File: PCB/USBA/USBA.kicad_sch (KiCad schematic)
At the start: 19 parts, among them J1 USB_A, J2 Shelly, U1 ESP32-PICO-MINI-02, U2 LMR16006+FB, U4 QR

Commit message: New layout for production
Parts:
- removed D1: RGB, RevK:LED-RGB-1.6x1.6, symbol Device:LED_ARGB
- removed U2: LMR16006+FB, RevK:SOT-23-Thin-6-Reg, symbol RevK:LMR16006+FB
- added D1: LED_BARG, RevK:MHS190RGBCT, symbol Device:LED_BARG
- added U2: LMR16006YDDCR, RevK:SOT-23-Thin-6-Reg, symbol RevK:LMR16006XDDCR
- C1: value 0.1uF -> 100nF; LCSC Part # (none) -> C30926; Part No 0603-100nF-50V -> (none)
- C2: LCSC Part # (none) -> C19110; Note 0603 or 0805 -> (none); Part No 0805-2.2uF-25V -> (none)
- C3: LCSC Part # (none) -> C17024; Note 0603 or 0805 -> (none); Part No 0805-10uF-16V -> (none)
- D2: JLCPCB Rotation Offset (none) -> 0; LCSC Part # (none) -> C143805; Part No CD1206-B2100 -> (none)
- J1, U4: now left out of the parts list
- L1: LCSC Part # (none) -> C354575; Manufacturer Laird -> (none); Part No TYA40206R8M-10 -> (none)
- R1: value 680R -> 300R; Part No (none) -> 0603-680R
- R2: value 2K -> 1K; Part No (none) -> 0603-2K
- R3: value 330R -> 100R; Part No (none) -> 0603-220R
- R4: value 100k 1% or 0R -> 100k 1%; LCSC Part # (none) -> C14675; Part No 0603-100k -> (none)
- R5: value 30k 1% or NF -> 30k 1%; LCSC Part # (none) -> C100001; Part No 0603-30k -> (none)
- U1: JLCPCB Rotation Offset (none) -> 180; LCSC Part # (none) -> C2980306
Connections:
- net +3.3V: now also D1.2 (A), U2.7 (VOUT)
- net GND: now also U2.2 (GND)
- net at R3.1: now also D1.1 (BK)
- net at R1.1: now also D1.3 (RK)
- net at R2.1: now also D1.4 (GK)
- net at R4.2, R5.2: now also U2.3 (FB)
- net VBUS renamed DC
- net DC: now also U2.4 (SHDN), U2.5 (VIN)
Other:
- moved on the sheet: C5, J1, J2, R6, U1

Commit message: Tidy
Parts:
- C5: value 10nF -> 1uF

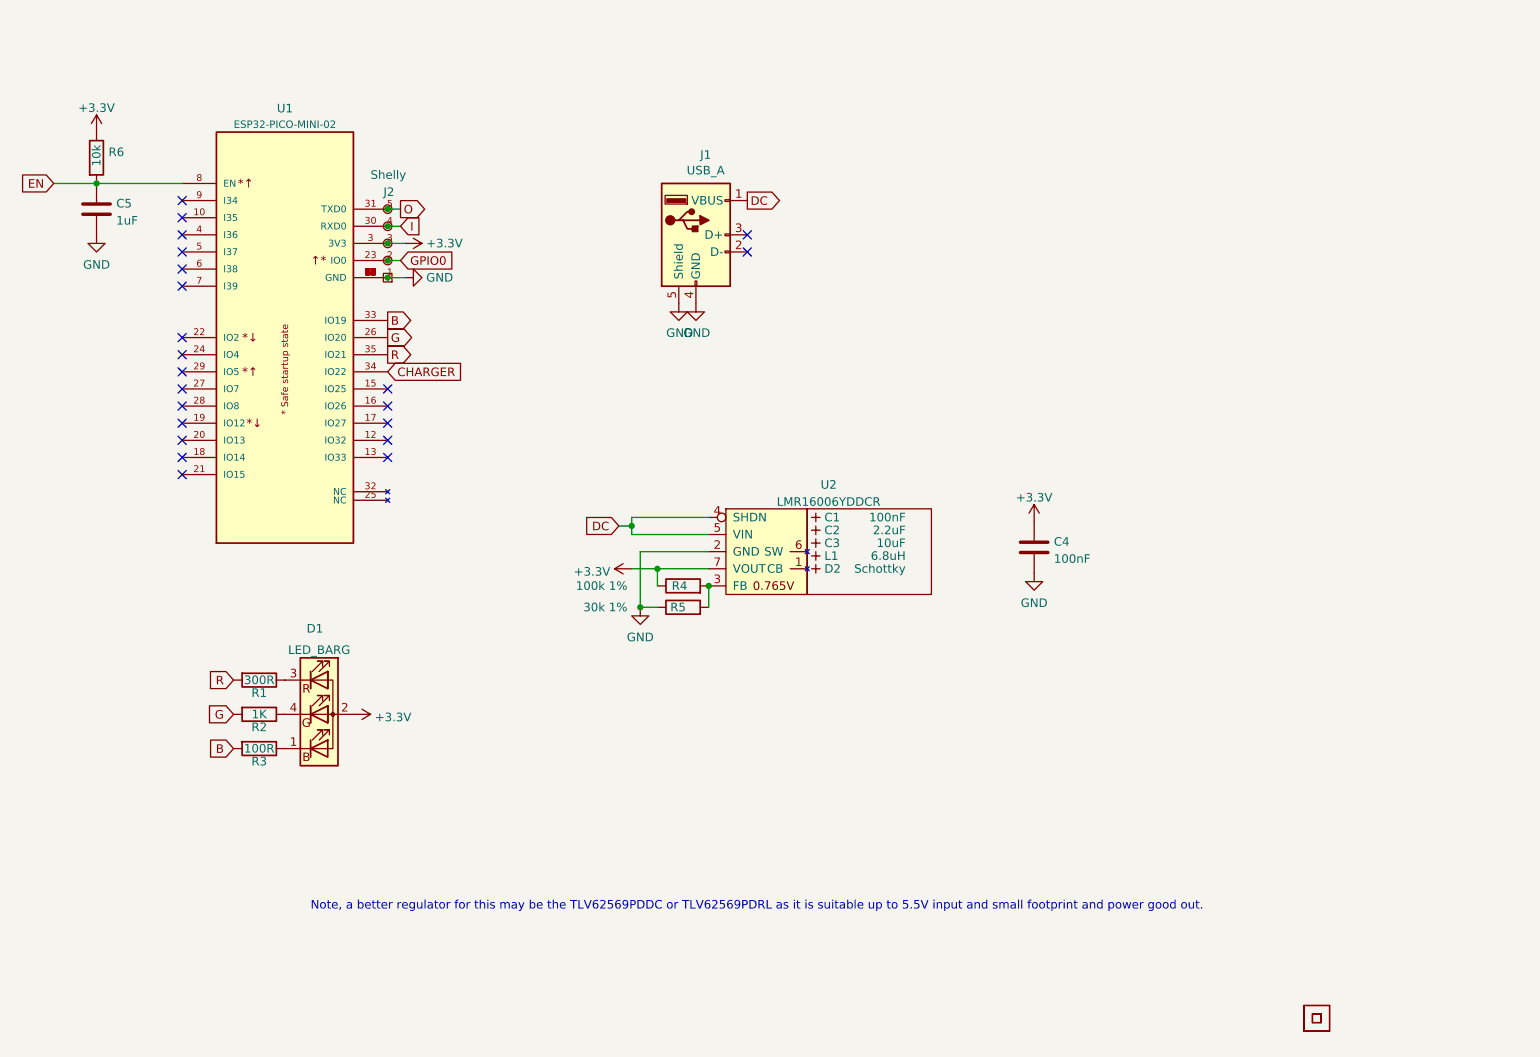
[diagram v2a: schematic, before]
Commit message: USBA as latest, and improve silk screen
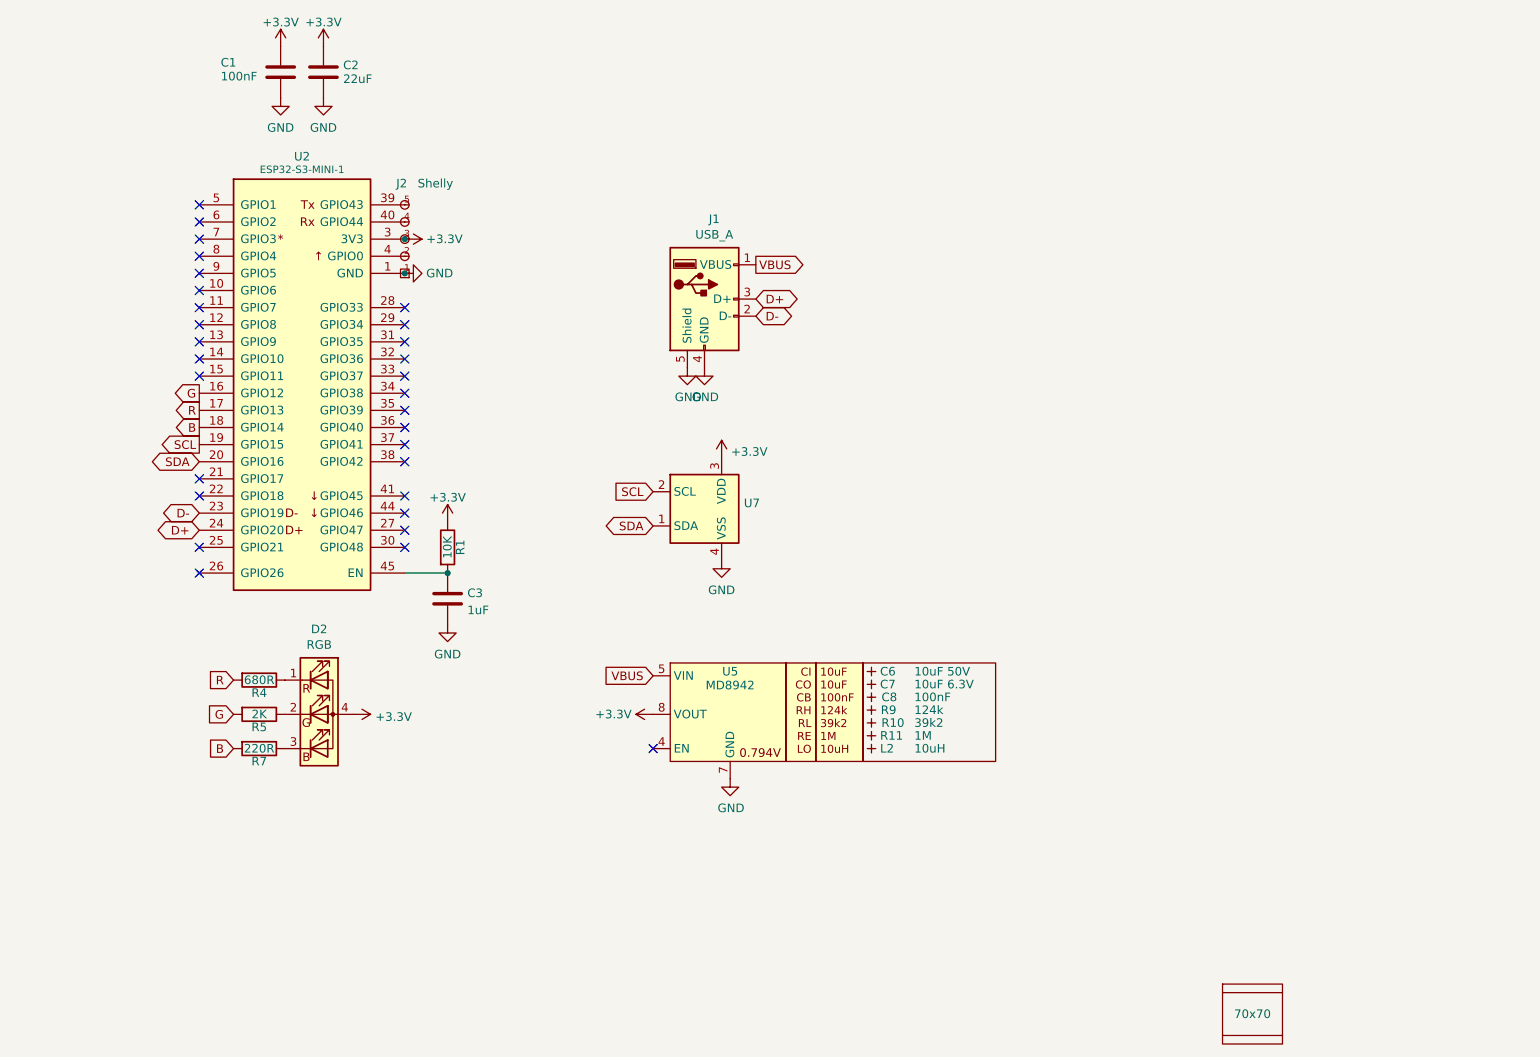
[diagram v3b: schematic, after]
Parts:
- removed C1: 100nF, RevK:C_0603_, symbol RevK:Hidden
- removed C2: 2.2uF, RevK:C_0805_, symbol RevK:Hidden
- removed C3: 10uF, RevK:C_0805_, symbol RevK:Hidden
- removed C4: 100nF, RevK:C_0603, symbol Device:C
- removed C5: 1uF, RevK:C_0603, symbol Device:C
- removed D1: LED_BARG, RevK:MHS190RGBCT, symbol Device:LED_BARG
- removed D2: Schottky, RevK:D_1206_, symbol RevK:Hidden
- removed L1: 6.8uH, RevK:L_4x4_, symbol RevK:Hidden
- removed R2: 1K, RevK:R_0603, symbol Device:R
- removed R3: 100R, RevK:R_0603, symbol Device:R
- removed R6: 10k, RevK:R_0603, symbol Device:R
- removed U1: ESP32-PICO-MINI-02, RevK:ESP32-PICO-MINI-02, symbol RevK:ESP32-PICO-MINI-02
- removed U2: LMR16006YDDCR, RevK:SOT-23-Thin-6-Reg, symbol RevK:LMR16006XDDCR
- removed U4: QR, RevK:QR-GENERIC, symbol RevK:QR
- added C1: 100nF, RevK:C_0402, symbol Device:C
- added C2: 22uF, RevK:C_0402, symbol Device:C
- added C3: 1uF, RevK:C_0402, symbol Device:C
- added C6: 10uF 50V, RevK:C_0603_, symbol RevK:Hidden
- added C7: 10uF 6.3V, RevK:C_0603_, symbol RevK:Hidden
- added C8: 100nF, RevK:C_0603_, symbol RevK:Hidden
- added D2: RGB, RevK:LED-RGB-1.6x1.6, symbol Device:LED_RGBA
- added L2: 10uH, RevK:L_4x4_, symbol RevK:Hidden
- added PCB1: 70x70, RevK:PCB7070, symbol RevK:PCB
- added R10: 39k2, RevK:R_0402_, symbol RevK:Hidden
- added R11: 1M, RevK:R_0402_, symbol RevK:Hidden
- added R7: 220R, RevK:R_0402, symbol Device:R
- added R9: 124k, RevK:R_0402_, symbol RevK:Hidden
- added U2: ESP32-S3-MINI-1, RevK:ESP32-S3-MINI-1, symbol RevK:ESP32-S3-MINI-1-N4R2
- added U5: MD8942, RevK:SOT-23-6-MD8942, symbol RevK:MD89420-RegBlock
- added U7: SHT40, RevK:Sensirion_DFN-4_1.5x1.5mm_P0.5mm_SHT4x, symbol RevK:SHT40
- added V1, V2: 70, RevK:VCUT70, symbol RevK:VCUT
- R1: value 300R -> 10K; footprint RevK:R_0603 -> RevK:R_0402; Part No 0603-680R -> (none)
- R4: value 100k 1% -> 680R; footprint RevK:R_0603 -> RevK:R_0402; LCSC Part # C14675 -> (none)
- R5: value 30k 1% -> 2K; footprint RevK:R_0603 -> RevK:R_0402; LCSC Part # C100001 -> (none)
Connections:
- net +3.3V: now also R1.1, C1.1, C2.1, D2.4 (A), U2.3 (3V3), U5.8 (VOUT), U7.3 (VDD); no longer R4.1
- net B: now also R7.2, U2.18 (GPIO14)
- net G: now also R5.2, U2.16 (GPIO12)
- net GND: now also C1.2, C2.2, C3.2, U2.1 (GND), U2.2 (GND), U2.42 (GND), U2.43 (GND), U2.46 (GND), U2.47 (GND), U2.48 (GND), U2.49 (GND), U2.50 (GND), U2.51 (GND), U2.52 (GND), U2.53 (GND), U2.54 (GND), U2.55 (GND), U2.56 (GND), U2.57 (GND), U2.58 (GND), U2.59 (GND), U2.60 (GND), U2.61 (GND), U2.62 (GND), U2.63 (GND), U2.64 (GND), U2.65 (GND), U5.2 (GND), U5.7 (GND), U7.4 (VSS); no longer R5.1
- net R: now also R4.2, U2.17 (GPIO13); no longer R1.2
- net D-: now reaches J1.2 (D-)
- net D-: now also U2.23 (GPIO19)
- net D+: now reaches J1.3 (D+)
- net D+: now also U2.24 (GPIO20)
- net DC renamed VBUS
- net VBUS: now also U5.5 (VIN)
- net GPIO0: no longer names the net of J2.2 (0)
- net GPIO0: now also U2.4 (GPIO0)
- net I: no longer names the net of J2.4 (Rx)
- net I: now also U2.40 (GPIO44)
- net O: no longer names the net of J2.5 (Tx)
- net O: now also U2.39 (GPIO43)
- new net: D2.1 (RK), R4.1
- new net: D2.2 (GK), R5.1
- new net: D2.3 (BK), R7.1
- new net: C3.1, R1.2, U2.45 (EN)
- new net SCL: U2.19 (GPIO15), U7.2 (SCL)
- new net SDA: U2.20 (GPIO16), U7.1 (SDA)
- no-connect marks 22 -> 30
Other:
- note removed: "Note, a better regulator for this may be the TLV62569PDDC or TLV62569PDRL as it is suitable up to 5.5V input and small footprint and power good out."
- moved on the sheet: J1

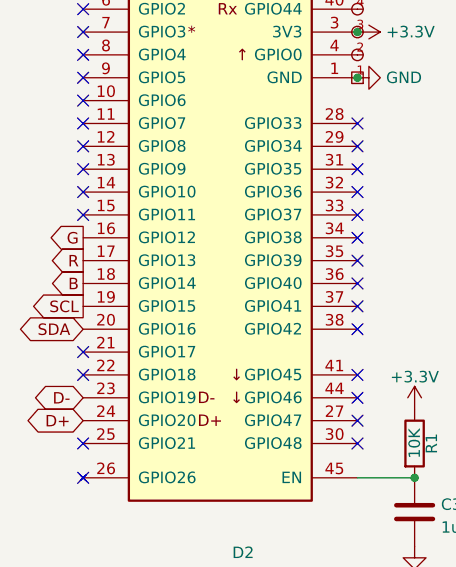
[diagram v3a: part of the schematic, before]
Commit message: Smaller footprint
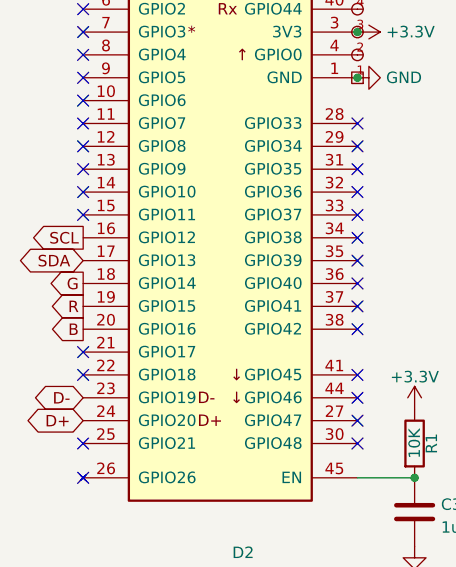
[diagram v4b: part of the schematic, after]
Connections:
- net B: now also U2.20 (GPIO16); no longer U2.18 (GPIO14)
- net G: now also U2.18 (GPIO14); no longer U2.16 (GPIO12)
- net R: now also U2.19 (GPIO15); no longer U2.17 (GPIO13)
- net SCL: now also U2.16 (GPIO12); no longer U2.19 (GPIO15)
- net SDA: now also U2.17 (GPIO13); no longer U2.20 (GPIO16)
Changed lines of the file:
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@@
     )
   )
-  (global_label "B" (shape output) (at 93.98 85.725 180) (fields_autoplaced)
+  (global_label "B" (shape output) (at 93.98 90.805 180) (fields_autoplaced)
     (effects (font (size 1.27 1.27)) (justify right))
-    (property "Intersheetrefs" "${INTERSHEET_REFS}" (at 90.4584 85.725 0)
+    (property "Intersheetrefs" "${INTERSHEET_REFS}" (at 90.4584 90.805 0)
       (effects (font (size 1.27 1.27)) (justify right) hide)
     )
@@
     )
   )
-  (global_label "G" (shape output) (at 93.98 80.645 180) (fields_autoplaced)
+  (global_label "G" (shape output) (at 93.98 85.725 180) (fields_autoplaced)
     (effects (font (size 1.27 1.27)) (justify right))
-    (property "Intersheetrefs" "${INTERSHEET_REFS}" (at 90.4584 80.645 0)
+    (property "Intersheetrefs" "${INTERSHEET_REFS}" (at 90.4584 85.725 0)
       (effects (font (size 1.27 1.27)) (justify right) hide)
     )
@@
     )
   )
-  (global_label "SCL" (shape output) (at 93.98 88.265 180) (fields_autoplaced)
+  (global_label "SCL" (shape output) (at 93.98 80.645 180) (fields_autoplaced)
     (effects (font (size 1.27 1.27)) (justify right))
-    (property "Intersheetrefs" "${INTERSHEET_REFS}" (at 88.2208 88.265 0)
+    (property "Intersheetrefs" "${INTERSHEET_REFS}" (at 88.2208 80.645 0)
       (effects (font (size 1.27 1.27)) (justify right) hide)
     )
@@
     )
   )
-  (global_label "SDA" (shape bidirectional) (at 93.98 90.805 180) (fields_autoplaced)
+  (global_label "SDA" (shape bidirectional) (at 93.98 83.185 180) (fields_autoplaced)
     (effects (font (size 1.27 1.27)) (justify right))
-    (property "Intersheetrefs" "${INTERSHEET_REFS}" (at 88.0877 90.7256 0)
+    (property "Intersheetrefs" "${INTERSHEET_REFS}" (at 88.0877 83.1056 0)
       (effects (font (size 1.27 1.27)) (justify right) hide)
     )
   )
-  (global_label "R" (shape output) (at 93.98 83.185 180) (fields_autoplaced)
+  (global_label "R" (shape output) (at 93.98 88.265 180) (fields_autoplaced)
     (effects (font (size 1.27 1.27)) (justify right))
-    (property "Intersheetrefs" "${INTERSHEET_REFS}" (at 90.4584 83.185 0)
+    (property "Intersheetrefs" "${INTERSHEET_REFS}" (at 90.4584 88.265 0)
       (effects (font (size 1.27 1.27)) (justify right) hide)
     )

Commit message: New reg
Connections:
- net GND: now also U2.21 (GPIO17), U2.22 (GPIO18)
- no-connect marks 30 -> 28
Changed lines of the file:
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@@
   (no_connect (at 124.46 100.965))
   (no_connect (at 124.46 103.505))
-  (no_connect (at 93.98 93.345))
   (no_connect (at 124.46 83.185))
   (no_connect (at 93.98 55.245))
@@
   (no_connect (at 124.46 73.025))
   (no_connect (at 93.98 62.865))
-  (no_connect (at 93.98 95.885))
   (no_connect (at 93.98 52.705))
   (no_connect (at 93.98 70.485))
@@
     )
   )
+  (symbol (lib_id "power:GND") (at 93.98 93.345 270) (unit 1)
+    (in_bom yes) (on_board yes) (dnp no) (fields_autoplaced)
+    (property "Reference" "#PWR014" (at 87.63 93.345 0)
+      (effects (font (size 1.27 1.27)) hide)
+    )
+    (property "Value" "GND" (at 90.8051 93.345 90)
+      (effects (font (size 1.27 1.27)) (justify right))
+    )
+    (property "Footprint" "" (at 93.98 93.345 0)
+      (effects (font (size 1.27 1.27)) hide)
+    )
+    (property "Datasheet" "" (at 93.98 93.345 0)
+      (effects (font (size 1.27 1.27)) hide)
+    )
+    (pin "1")
+    (instances
+      (project "USBA"
+        (path "/2d210a96-f81f-42a9-8bf4-1b43c11086f3"
+          (reference "#PWR014") (unit 1)
+        )
+      )
+    )
+  )
   (symbol (lib_id "RevK:PCB") (at 250.19 172.72 0) (unit 1)
     (in_bom no) (on_board yes) (dnp no)
@@
         )
       )
+    )
+  )
+  (symbol (lib_id "power:GND") (at 93.98 95.885 270) (unit 1)
+    (in_bom yes) (on_board yes) (dnp no) (fields_autoplaced)
+    (property "Reference" "#PWR015" (at 87.63 95.885 0)
+      (effects (font (size 1.27 1.27)) hide)
+    )
+    (property "Value" "GND" (at 90.8051 95.885 90)
+      (effects (font (size 1.27 1.27)) (justify right))
+    )
+    (property "Footprint" "" (at 93.98 95.885 0)
+      (effects (font (size 1.27 1.27)) hide)
+    )
+    (property "Datasheet" "" (at 93.98 95.885 0)
+      (effects (font (size 1.27 1.27)) hide)
+    )
+    (pin "1")
+    (instances
+      (project "USBA"
+        (path "/2d210a96-f81f-42a9-8bf4-1b43c11086f3"
+          (reference "#PWR015") (unit 1)
+        )
+      )

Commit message: Tidy
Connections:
- net GND: no longer U2.21 (GPIO17), U2.22 (GPIO18)
- no-connect marks 28 -> 30
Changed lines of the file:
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@@
   (no_connect (at 93.98 73.025))
   (no_connect (at 93.98 78.105))
+  (no_connect (at 93.98 93.345))
   (no_connect (at 124.46 67.945))
   (no_connect (at 124.46 90.805))
@@
   (no_connect (at 93.98 67.945))
   (no_connect (at 93.98 60.325))
+  (no_connect (at 93.98 95.885))
   (no_connect (at 93.98 107.315))
   (no_connect (at 93.98 75.565))
@@
     )
   )
-  (symbol (lib_id "power:GND") (at 93.98 93.345 270) (unit 1)
-    (in_bom yes) (on_board yes) (dnp no) (fields_autoplaced)
-    (property "Reference" "#PWR014" (at 87.63 93.345 0)
-      (effects (font (size 1.27 1.27)) hide)
-    )
-    (property "Value" "GND" (at 90.8051 93.345 90)
-      (effects (font (size 1.27 1.27)) (justify right))
-    )
-    (property "Footprint" "" (at 93.98 93.345 0)
-      (effects (font (size 1.27 1.27)) hide)
-    )
-    (property "Datasheet" "" (at 93.98 93.345 0)
-      (effects (font (size 1.27 1.27)) hide)
-    )
-    (pin "1")
-    (instances
-      (project "USBA"
-        (path "/2d210a96-f81f-42a9-8bf4-1b43c11086f3"
-          (reference "#PWR014") (unit 1)
-        )
-      )
-    )
-  )
   (symbol (lib_id "RevK:PCB") (at 250.19 172.72 0) (unit 1)
     (in_bom no) (on_board yes) (dnp no)
@@
         )
       )
-    )
-  )
-  (symbol (lib_id "power:GND") (at 93.98 95.885 270) (unit 1)
-    (in_bom yes) (on_board yes) (dnp no) (fields_autoplaced)
-    (property "Reference" "#PWR015" (at 87.63 95.885 0)
-      (effects (font (size 1.27 1.27)) hide)
-    )
-    (property "Value" "GND" (at 90.8051 95.885 90)
-      (effects (font (size 1.27 1.27)) (justify right))
-    )
-    (property "Footprint" "" (at 93.98 95.885 0)
-      (effects (font (size 1.27 1.27)) hide)
-    )
-    (property "Datasheet" "" (at 93.98 95.885 0)
-      (effects (font (size 1.27 1.27)) hide)
-    )
-    (pin "1")
-    (instances
-      (project "USBA"
-        (path "/2d210a96-f81f-42a9-8bf4-1b43c11086f3"
-          (reference "#PWR015") (unit 1)
-        )
-      )
